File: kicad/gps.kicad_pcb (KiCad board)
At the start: 2 copper layers, 84.6 x 64 mm, 1 part, among them J1 Bus_PCI_Express_x1

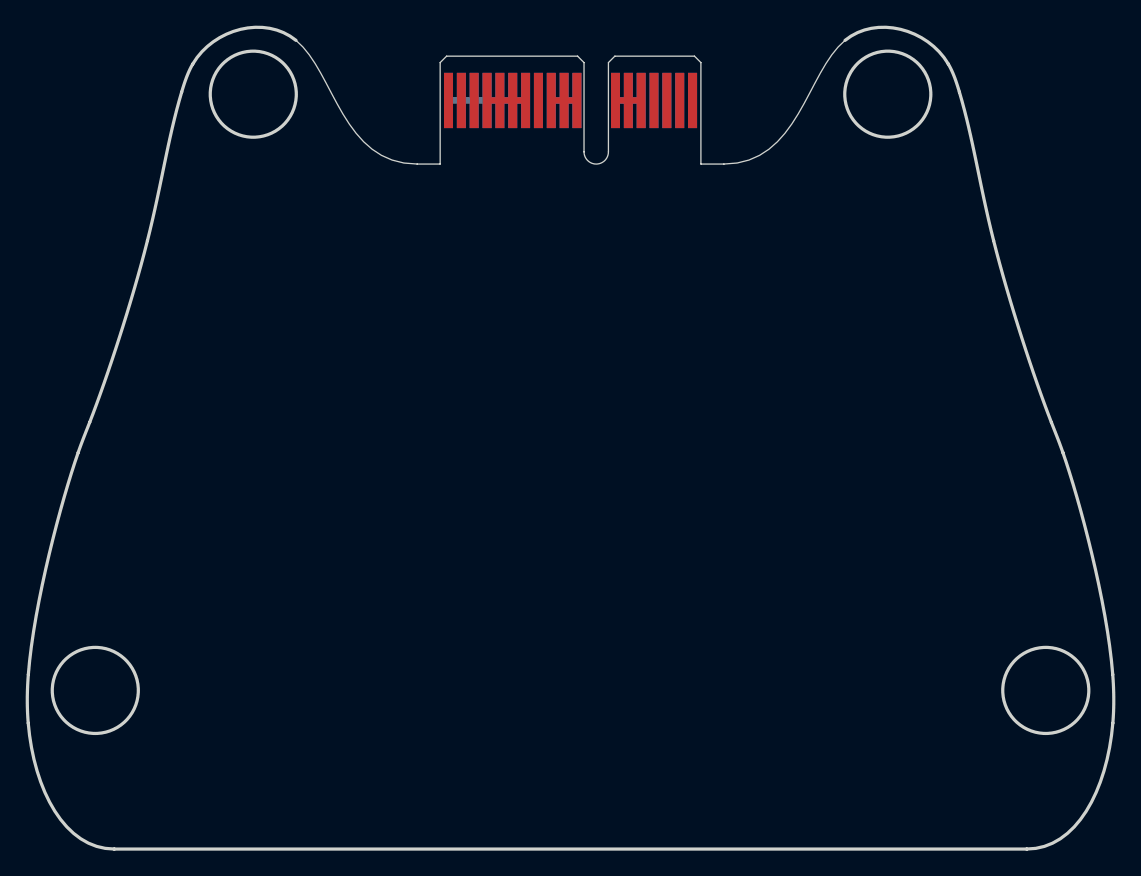
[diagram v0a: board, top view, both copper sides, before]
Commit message: Update footprint to match sensor 0.2.0
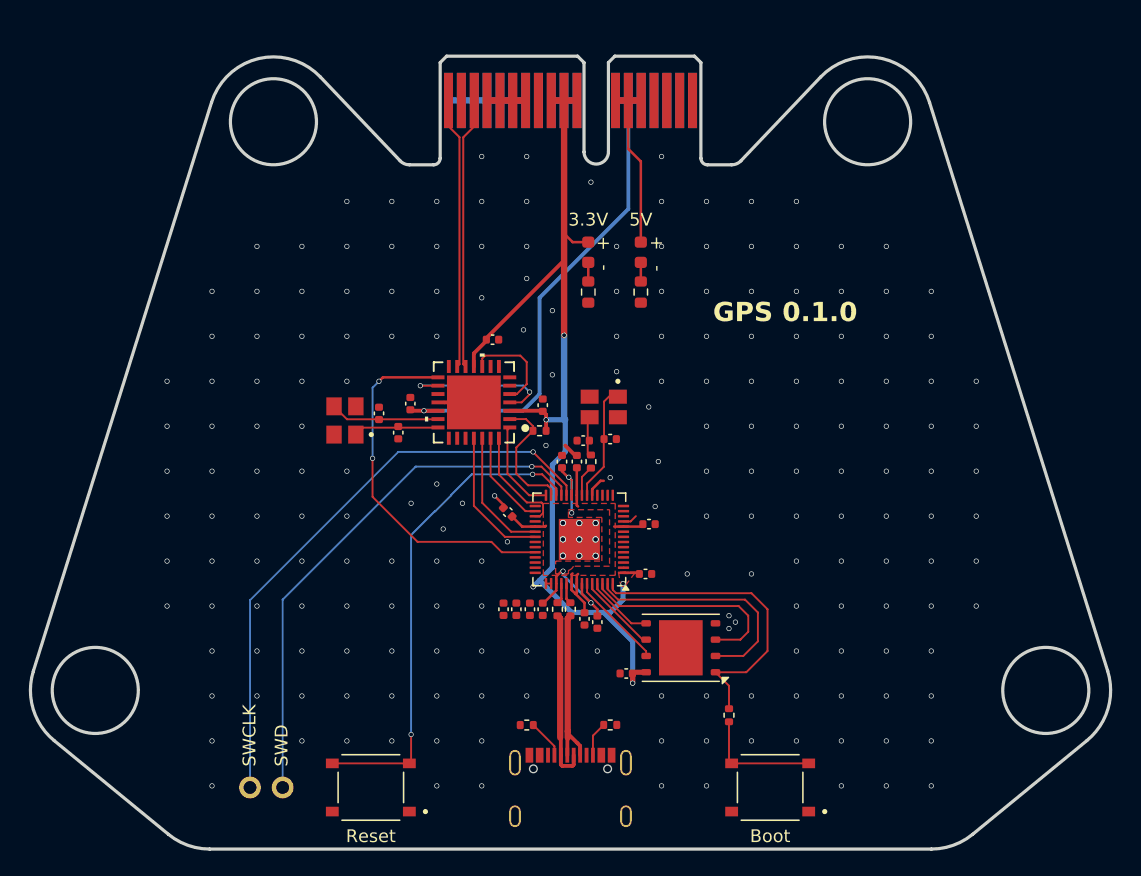
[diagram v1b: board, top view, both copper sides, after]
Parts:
- added C10: 15p, Capacitor_SMD:C_0402_1005Metric, F.Cu at (149.5, 90.5)
- added C11: 15p, Capacitor_SMD:C_0402_1005Metric, F.Cu at (147.4, 90.6)
- added C206: 100n, Capacitor_SMD:C_0402_1005Metric, F.Cu at (148.5, 104.8)
- added C207: 100n, Capacitor_SMD:C_0402_1005Metric, F.Cu at (145.8, 92.2)
- added C208: 1u, Capacitor_SMD:C_0402_1005Metric, F.Cu at (144.2, 103.8)
- added C209: 100n, Capacitor_SMD:C_0402_1005Metric, F.Cu at (147.5, 104.5)
- added C210: 1u, Capacitor_SMD:C_0402_1005Metric, F.Cu at (143.2, 103.8)
- added C211: 100n, Capacitor_SMD:C_0402_1005Metric, F.Cu at (152.2, 101.0)
- added C212: 100n, Capacitor_SMD:C_0402_1005Metric, F.Cu at (141.5, 96.2)
- added C213: 100n, Capacitor_SMD:C_0402_1005Metric, F.Cu at (152.5, 97.1)
- added C214: 100n, Capacitor_SMD:C_0402_1005Metric, F.Cu at (146.9, 92.3)
- added C215: 100n, Capacitor_SMD:C_0402_1005Metric, F.Cu at (141.2, 103.7)
- added C216: 100n, Capacitor_SMD:C_0402_1005Metric, F.Cu at (142.2, 103.7)
- added C40: 100n, Capacitor_SMD:C_0402_1005Metric, F.Cu at (150.8, 108.8)
- added C90: 100n, Capacitor_SMD:C_0402_1005Metric, F.Cu at (140.3, 82.8)
- added C92: 100n, Capacitor_SMD:C_0402_1005Metric, F.Cu at (144.2, 87.9)
- added C93: 100n, Capacitor_SMD:C_0402_1005Metric, F.Cu at (133.9, 87.7)
- added C94: 22p, Capacitor_SMD:C_0402_1005Metric, F.Cu at (133.0, 90.0)
- added C95: 22p, Capacitor_SMD:C_0402_1005Metric, F.Cu at (131.5, 88.5)
- added D1: LED, LED_SMD:LED_0603_1608Metric, F.Cu at (147.8, 76.0)
- added D2: LED, LED_SMD:LED_0603_1608Metric, F.Cu at (151.9, 76.0)
- added J4: Conn_01x02, Connector_PinHeader_2.54mm:PinHeader_1x02_P2.54mm_Vertical, F.Cu at (121.5, 117.6)
- added J6: USB_C_Receptacle_USB2.0_16P, Connector_USB:USB_C_Receptacle_Palconn_UTC16-G, F.Cu at (146.4, 117.6)
- added R1: 150, Resistor_SMD:R_0603_1608Metric, F.Cu at (147.8, 79.1)
- added R12: 1k, Resistor_SMD:R_0402_1005Metric, F.Cu at (148.0, 92.2)
- added R2: 150, Resistor_SMD:R_0603_1608Metric, F.Cu at (151.9, 79.1)
- added R203: 27, Resistor_SMD:R_0402_1005Metric, F.Cu at (146.4, 103.8)
- added R204: 27, Resistor_SMD:R_0402_1005Metric, F.Cu at (145.4, 103.8)
- added R3: 5.1k, Resistor_SMD:R_0402_1005Metric, F.Cu at (149.5, 112.8)
- added R30: 1k, Resistor_SMD:R_0402_1005Metric, F.Cu at (158.8, 112.0)
- added R4: 5.1k, Resistor_SMD:R_0402_1005Metric, F.Cu at (143.0, 112.8)
- added R91: 10k, Resistor_SMD:R_0402_1005Metric, F.Cu at (144.0, 89.9)
- added S1: TS-1187A-B-A-B, TS-1187A-B-A-B:SW_TS-1187A-B-A-B, F.Cu at (162.0, 117.6)
- added S2: TS-1187A-B-A-B, TS-1187A-B-A-B:SW_TS-1187A-B-A-B, F.Cu at (130.9, 117.6)
- added U2: RP2040, Package_DFN_QFN:QFN-56-1EP_7x7mm_P0.4mm_EP3.2x3.2mm, F.Cu at (147.1, 98.3)
- added U4: W25Q128JVP, Package_SON:WSON-8-1EP_6x5mm_P1.27mm_EP3.4x4.3mm, F.Cu at (155.0, 106.8)
- added U9: MCP25625T-E/ML, MCP25625T_E_ML:QFN28_6X6MC_MCH, F.Cu at (138.9, 87.6)
- added X1: ABM8-272-T3, ABM8-272-T3:ABM8-272-T3_ABR, F.Cu at (149.0, 88.0)
- added Y2: X322516MLB4SI, X322516MLB4SI:OSC_X322516MLB4SI, F.Cu at (128.8, 89.1)
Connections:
- J1 pad A16: +7.4V -> unconnected-(J1-PERp0-PadA16)
- J1 pad A17: +7.4V -> unconnected-(J1-PERn0-PadA17)
- J1 pad A18: +7.4V -> unconnected-(J1-GND-PadA18)
- J1 pad B16: +7.4V -> unconnected-(J1-GND-PadB16)
- J1 pad B17: +7.4V -> unconnected-(J1-~{PRSNT2}-PadB17)
- J1 pad B18: +7.4V -> unconnected-(J1-GND-PadB18)
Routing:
- net +3.3V: track 4.00 -> 101.3 mm, vias 0 -> 5
- net +5V: track 3.71 -> 52.6 mm, vias 0 -> 1
- net /SWCLK: track 0.00 -> 45.9 mm, vias 0 -> 1
- net /SWD: track 0.00 -> 41.8 mm, vias 0 -> 1
- net /RUN: track 0.00 -> 38.0 mm, vias 0 -> 2
- net CANSTBY: track 0.00 -> 28.4 mm, vias 0 -> 2
- net /QSPI_SS: track 0.00 -> 24.4 mm
- net CANP: track 2.01 -> 21.1 mm
- net CANN: track 2.02 -> 21.1 mm
- net /QSPI_SD1: track 0.00 -> 18.9 mm
- net /QSPI_SD2: track 0.00 -> 16.7 mm
- net +1.1V: track 0.00 -> 15.0 mm, vias 0 -> 4
- net USB_D-: track 0.00 -> 13.4 mm
- net USB_D+: track 0.00 -> 13.2 mm
- net tx: track 0.00 -> 12.1 mm, vias 0 -> 2
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- added copper zone on F.Cu, net +1.1V
- added copper zone on F.Cu, net +3.3V
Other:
- board size 84.6 x 64 mm -> 84.1 x 61.7 mm
- board text added: "3.3V"
- board text added: "5V"
- board text added: "Boot"
- board text added: "GPS 0.1.0"
- board text added: "Reset"
- board text added: "SWCLK"
- board text added: "SWD"

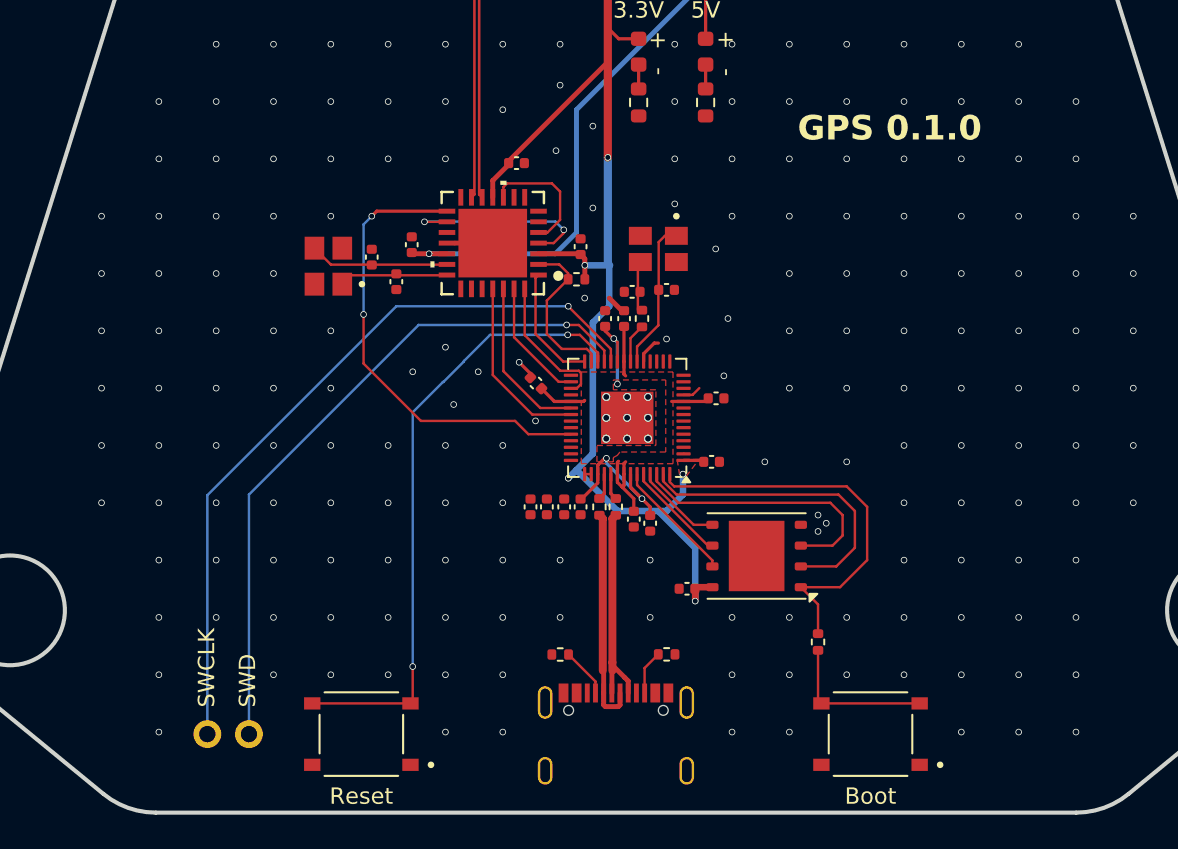
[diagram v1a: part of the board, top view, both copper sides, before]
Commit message: Switch from MAX M10S to NEO-M9N for enhanced GPS performance
Switched from MAX M10S to NEO-M9N for improved GPS preformance. The NEO-M9N offers faster position acquisition with concurrent GNSS support (GPS, Galileo, GLONASS, BeiDou), higher accuracy, and up to 25 Hz update rates.
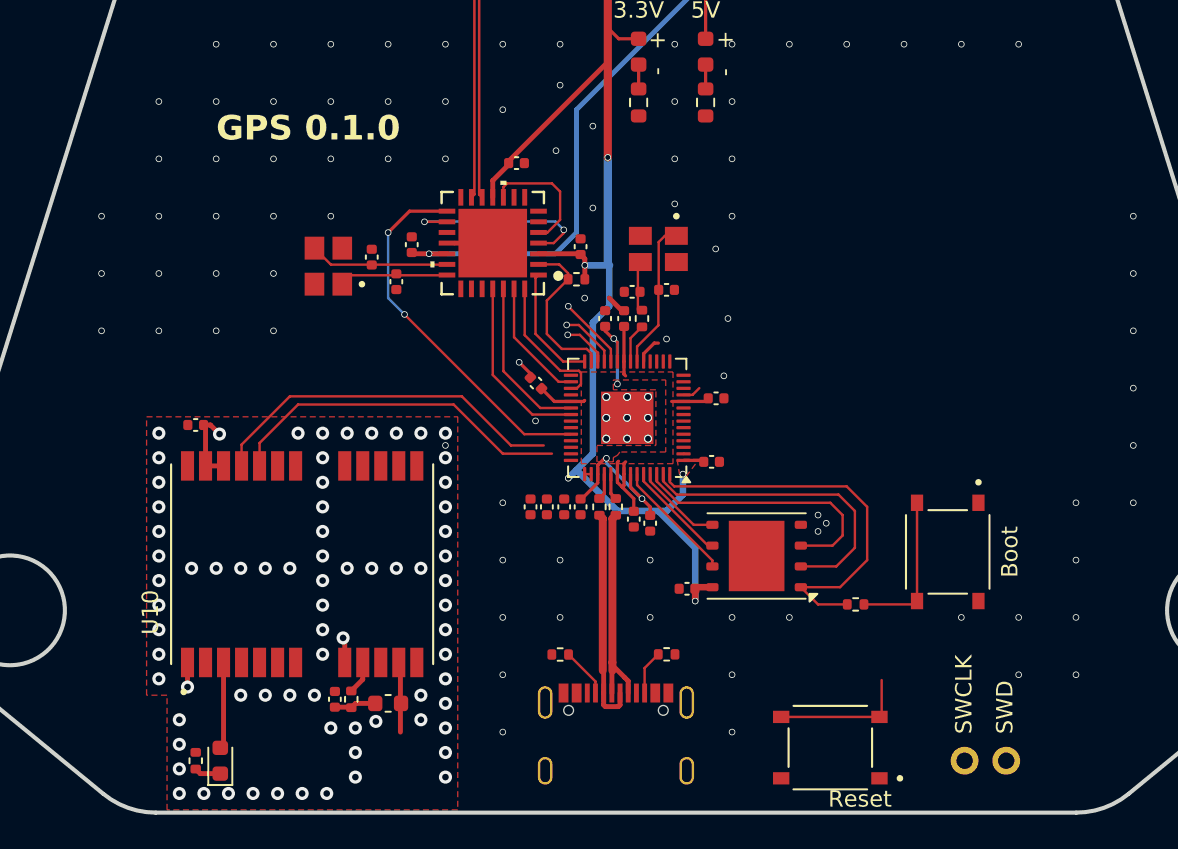
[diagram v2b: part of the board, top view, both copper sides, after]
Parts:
- added C32: 100n 10% 16V X7R, Capacitor_SMD:C_0402_1005Metric, F.Cu at (129.2, 115.5)
- added C33: 100n, Capacitor_SMD:C_0402_1005Metric, F.Cu at (120.8, 98.8)
- added D2: BLUE, LED_SMD:LED_0603_1608Metric, F.Cu at (122.2, 119.2)
- added L5: 27n >300mA, Inductor_SMD:L_0603_1608Metric, F.Cu at (132.5, 115.8)
- added R3: 10R, Resistor_SMD:R_0402_1005Metric, F.Cu at (130.2, 115.5)
- added R4: 1k, Resistor_SMD:R_0402_1005Metric, F.Cu at (120.8, 119.2)
- added U10: NEO-M9N, GPSLIB:XCVR_NEO-M9N-00B, F.Cu at (127.2, 107.2)
- moved J4 46.3 mm to (167.7, 119.2)
- moved S2 28.6 mm to (159.5, 118.5)
- moved S1 12.1 mm to (166.7, 106.5), turned to -90 degrees
- moved R30 3.25 mm to (161.0, 109.7), turned to 0 degrees
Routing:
- net (no net): track 0.00 -> 65.8 mm, vias 0 -> 3
- net /SWCLK: track 45.9 -> 4.45 mm
- net /SWD: track 41.8 -> 3.52 mm
- net /RUN: track 38.0 -> 11.1 mm, vias 2 -> 1
- net CANSTBY: track 28.4 -> 22.7 mm
- net Net-(D2-K): track 1.49 -> 3.10 mm
- net GND: vias 210 -> 180
- added copper zone on F.Cu, net GND

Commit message: update pcb
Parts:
- removed C32: 100n 10% 16V X7R, Capacitor_SMD:C_0402_1005Metric
- removed C33: 100n, Capacitor_SMD:C_0402_1005Metric
- removed J4: Conn_01x02, Connector_PinHeader_2.54mm:PinHeader_1x02_P2.54mm_Vertical
- removed L5: 27n >300mA, Inductor_SMD:L_0603_1608Metric
- removed U10: NEO-M9N, GPSLIB:XCVR_NEO-M9N-00B
- added AE2: SMA-M, GPSLIB:SMA-EDGE, F.Cu at (228.9, 61.2)
- added B1: 6.8MM_COIN_CELL, GPSLIB:6.8mm-coincell-ML414H_IV01E, F.Cu at (236.5, 70.0)
- added C1: 100n, Capacitor_SMD:C_0402_1005Metric, F.Cu at (243.5, 59.0)
- added C22: 100n, Capacitor_SMD:C_0402_1005Metric, F.Cu at (228.4, 81.6)
- added C23: 100n 10% 16V X7R, Capacitor_SMD:C_0402_1005Metric, F.Cu at (236.9, 98.3)
- added C24: 1u, Capacitor_SMD:C_0402_1005Metric, F.Cu at (243.5, 62.9)
- added C25: 100n, Capacitor_SMD:C_0402_1005Metric, F.Cu at (243.5, 64.9)
- added C26: 100n, Capacitor_SMD:C_0402_1005Metric, F.Cu at (243.5, 66.9)
- added C27: 100n, Capacitor_SMD:C_0402_1005Metric, F.Cu at (246.4, 59.0)
- added C28: 1u, Capacitor_SMD:C_0402_1005Metric, F.Cu at (246.4, 61.0)
- added C29: 12p, Capacitor_SMD:C_0402_1005Metric, F.Cu at (246.4, 62.9)
- added C30: 12p, Capacitor_SMD:C_0402_1005Metric, F.Cu at (246.4, 64.9)
- added C31: 1u, Capacitor_SMD:C_0402_1005Metric, F.Cu at (246.4, 66.9)
- added C7: 1uF, Capacitor_SMD:C_0402_1005Metric, F.Cu at (243.5, 61.0)
- added D1: LED, LED_SMD:LED_0603_1608Metric, F.Cu at (230.1, 64.9)
- added D5: LED, LED_SMD:LED_0603_1608Metric, F.Cu at (229.9, 102.1)
- added D6: LED, LED_SMD:LED_0603_1608Metric, F.Cu at (230.1, 67.5)
- added J3: Conn_01x02, Connector_PinHeader_2.54mm:PinHeader_1x02_P2.54mm_Vertical, F.Cu at (121.5, 117.6)
- added L1: 27n >300mA, Inductor_SMD:L_0603_1608Metric, F.Cu at (240.2, 98.6)
- added PPS_LED1: JUMPER-SMT_2_NC_TRACE_SILK, GPSLIB:SMT-JUMPER_2_NC_TRACE_SILK, F.Cu at (226.2, 65.3)
- added PWR1: JUMPER-SMT_2_NC_TRACE_SILK, GPSLIB:SMT-JUMPER_2_NC_TRACE_SILK, F.Cu at (226.2, 68.5)
- added R1: 10k, Resistor_SMD:R_0402_1005Metric, F.Cu at (234.9, 51.0)
- added R18: 1k, Resistor_SMD:R_0402_1005Metric, F.Cu at (240.8, 51.0)
- added R19: 100k, Resistor_SMD:R_0402_1005Metric, F.Cu at (240.8, 53.0)
- added R2: 27, Resistor_SMD:R_0402_1005Metric, F.Cu at (234.9, 53.0)
- added R20: 1k, Resistor_SMD:R_0402_1005Metric, F.Cu at (240.8, 55.0)
- added R21: 10k, Resistor_SMD:R_0402_1005Metric, F.Cu at (240.8, 57.0)
- added R22: 1k, Resistor_SMD:R_0402_1005Metric, F.Cu at (228.4, 102.1)
- added R23: 100k, Resistor_SMD:R_0402_1005Metric, F.Cu at (243.7, 51.0)
- added R24: 10R, Resistor_SMD:R_0402_1005Metric, F.Cu at (237.9, 98.3)
- added R25: 100k, Resistor_SMD:R_0402_1005Metric, F.Cu at (243.7, 53.0)
- added R28: 100k, Resistor_SMD:R_0402_1005Metric, F.Cu at (243.7, 55.0)
- added R29: 10k, Resistor_SMD:R_0402_1005Metric, F.Cu at (243.7, 57.0)
- added R5: 1M, Resistor_SMD:R_0402_1005Metric, F.Cu at (237.8, 51.0)
- added R6: 12k, Resistor_SMD:R_0402_1005Metric, F.Cu at (237.8, 53.0)
- added R7: 1k, Resistor_SMD:R_0402_1005Metric, F.Cu at (237.8, 55.0)
- added R9: 3.3k, Resistor_SMD:R_0402_1005Metric, F.Cu at (237.8, 57.0)
- added TP1: TP_GNSS_SAFEBOOT, TestPoint:TestPoint_Pad_D1.0mm, F.Cu at (246.6, 51.6)
- added TP2: TP_GNSS_RST, TestPoint:TestPoint_Pad_D1.0mm, F.Cu at (246.6, 54.6)
- added U5: NEO-M9N, GPSLIB:XCVR_NEO-M9N-00B, F.Cu at (234.9, 90.1)
- added U6: USB2514B-AEZC-TR, GPSLIB:QFN36_6X6MC_MCH, F.Cu at (237.7, 62.4)
- added X2: 24MHz, GPSLIB:CRYSTAL-SMD_4P-L3.2-W2.5-BL, F.Cu at (244.9, 70.1)
- D2: value BLUE -> 0.5A/40V/420mV; footprint LED_SMD:LED_0603_1608Metric -> GPSLIB:SOD-323
- R3: value 10R -> 27
- R4: value 1k -> 10k
- moved R4 130.0 mm to (234.9, 57.0), turned to 0 degrees
- moved R3 120.9 mm to (234.9, 55.0), turned to 0 degrees
- moved D2 118.8 mm to (230.4, 70.2), turned to 0 degrees
- moved S2 28.6 mm to (130.9, 117.6)
- moved S1 12.1 mm to (162.0, 117.6), turned to 180 degrees
- moved R8 3.25 mm to (158.8, 112.0), turned to -90 degrees
- renumbered C208 to C10, C209 to C11, C210 to C12, C211 to C13, C93 to C14, C212 to C15, C94 to C16, C213 to C17, C214 to C18, C95 to C19, C40 to C2, C215 to C20, C216 to C21, C10 to C3, C11 to C4, C92 to C5, C90 to C6, C206 to C8, C207 to C9, D1 to D3, D2 to D4, J6 to J2, R1 to R10, R4 to R11, R3 to R12, R2 to R13, R12 to R14, R91 to R15, R203 to R16, R204 to R17, R30 to R8, U4 to U2, U9 to U3, U2 to U4, Y2 to Y1
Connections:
- net /USB_D2+ renamed Net-(U4-USB_DP)
- net /USB_D2- renamed Net-(U4-USB_DM)
- net BNORESET renamed /MOSI
- D4 pad 1: Net-(D2-K) -> Net-(D4-K)
- R13 pad 1: Net-(D2-K) -> Net-(D4-K)
- R16 pad 1: USB_D+ -> /USBDP_DN4
- R17 pad 1: USB_D- -> /USBDM_DN4
- R3 pad 1: (no net) -> /USBDP_DN1
- R3 pad 2: (no net) -> Net-(U5-USB_DP)
- R4 pad 1: Net-(D2-K) -> Net-(U6-OCS_N1)
- R4 pad 2: GND -> +3V3
- U4 pad 11: BOOT_LOAD -> unconnected-(U4-GPIO8-Pad11)
- U4 pad 2: unconnected-(U2-GPIO0-Pad2) -> USART4_TX
- U4 pad 3: unconnected-(U2-GPIO1-Pad3) -> USART4_RX
- U4 pad 39: BMPINT -> unconnected-(U4-GPIO27_ADC1-Pad39)
- U4 pad 4: SDA1 -> unconnected-(U4-GPIO2-Pad4)
- U4 pad 40: SDA0 -> unconnected-(U4-GPIO28_ADC2-Pad40)
- U4 pad 41: SCL0 -> unconnected-(U4-GPIO29_ADC3-Pad41)
- U4 pad 5: SCL1 -> unconnected-(U4-GPIO3-Pad5)
- U4 pad 6: unconnected-(U2-GPIO4-Pad6) -> /MISO
- U4 pad 7: unconnected-(U2-GPIO5-Pad7) -> CS
- U4 pad 8: BNOINT -> SCK
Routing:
- net (no net): track 65.8 -> 10.1 mm, vias 3 -> 1
- net /SWCLK: track 4.45 -> 45.9 mm
- net /SWD: track 3.52 -> 41.8 mm
- net /RUN: track 11.1 -> 38.0 mm, vias 1 -> 2
- net USART4_TX: track 0.00 -> 20.2 mm
- net USART4_RX: track 0.00 -> 18.5 mm
- net CANSTBY: track 22.7 -> 28.4 mm
- net Net-(AE2-SIGNAL): track 0.00 -> 4.29 mm
- net Net-(D2-K): track 3.10 -> 0.00 mm
- net Net-(C23-Pad1): track 0.00 -> 2.58 mm
- net +3.3V: track 101.3 -> 103.5 mm, vias 5 -> 12
- net Net-(U5-VCC_RF): track 0.00 -> 2.03 mm
- net GND: track 16.3 -> 17.9 mm, vias 180 -> 251
- net Net-(U5-~{RESET}): track 0.00 -> 1.54 mm, vias 0 -> 1
- net Net-(U5-~{SAFEBOOT}): track 0.00 -> 1.50 mm, vias 0 -> 1
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- added copper zone on B.Cu, net +3.3V
- added copper zone on B.Cu, net GND
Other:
- board text added: "sensors 0.2.0"
- board text removed: "GPS 0.1.0"

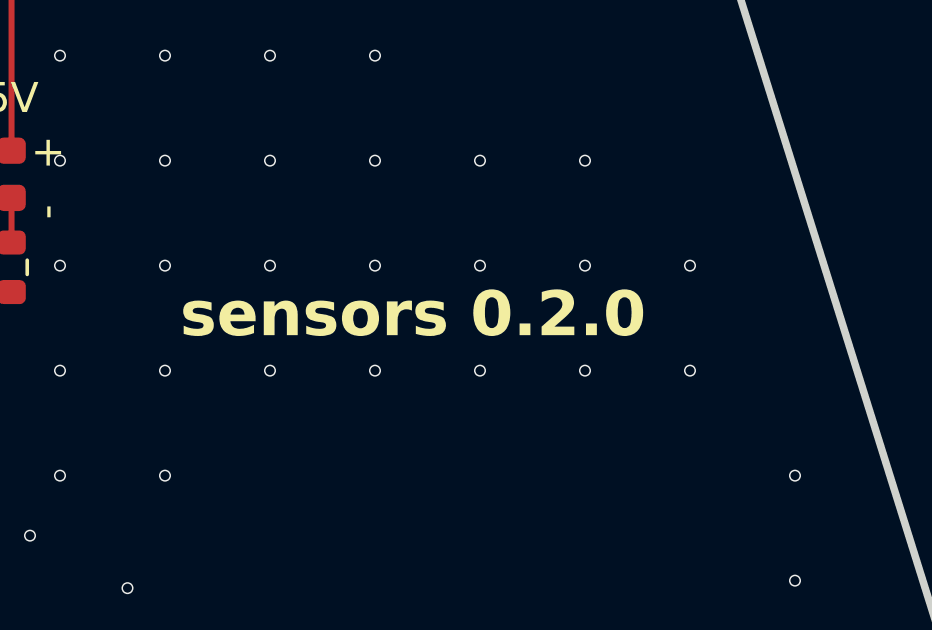
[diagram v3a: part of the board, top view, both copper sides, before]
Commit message: Remove outdated file gpsold
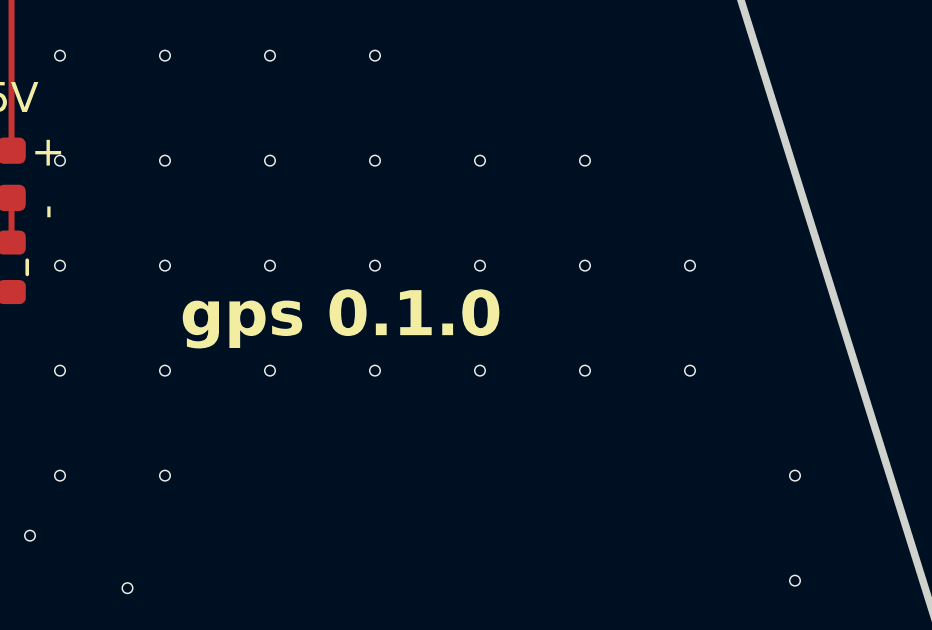
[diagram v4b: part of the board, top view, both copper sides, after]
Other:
- board text added: "gps 0.1.0"
- board text removed: "sensors 0.2.0"
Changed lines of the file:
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@@
 		(layer "Edge.Cuts")
 	)
-	(gr_text "sensors 0.2.0"
+	(gr_text "gps 0.1.0"
 		(at 157.5 81.5 0)
 		(layer "F.SilkS")
